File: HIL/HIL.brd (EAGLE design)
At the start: 129.1 x 103.9 mm, 245 parts, among them J1 JTAG_ARM_10PIN, J4 JTAG_ARM_10PIN, U1 CD74HC4067SM96, U10 INA219AIDCNR, U11 INA219AIDCNR, U12 INA219AIDCNR, U14 ADUM1201ARZ, U15 SN65HVD230D, U16 TL1963AKTTR., U17 FT230XS, U2 TL1963AKTTR., U3 CD74HC4067SM96, U4 CD74HC4067SM96, U5 MCP4725A0T-E/CH, U6 TL1963AKTTR., U7 MCP2003-E/SN, U8 TM4C1294NCPDT, U9 INA219AIDCNR, X1 A1944-50, X2 A1944-50, X4 A1944-50, Y3 NX3225GA

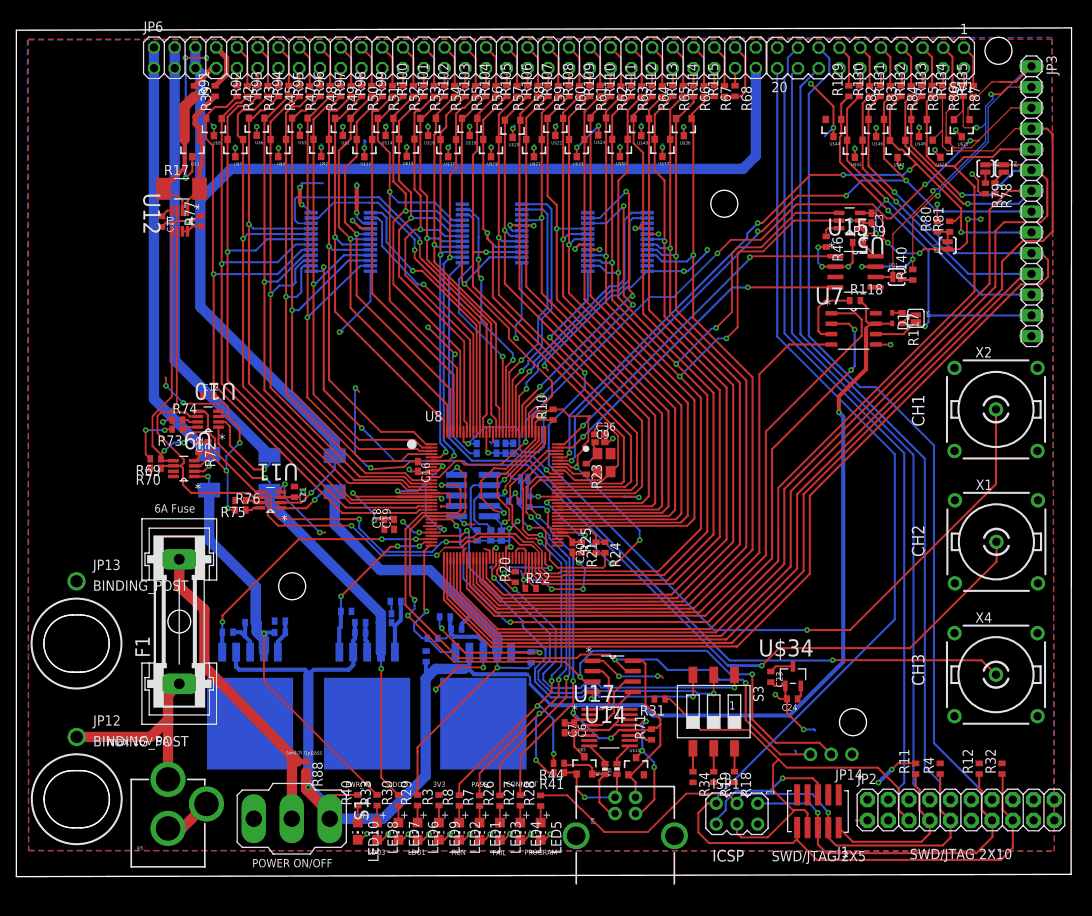
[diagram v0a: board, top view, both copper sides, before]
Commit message: Extend plane
Extend TSTR_3V3’s plane
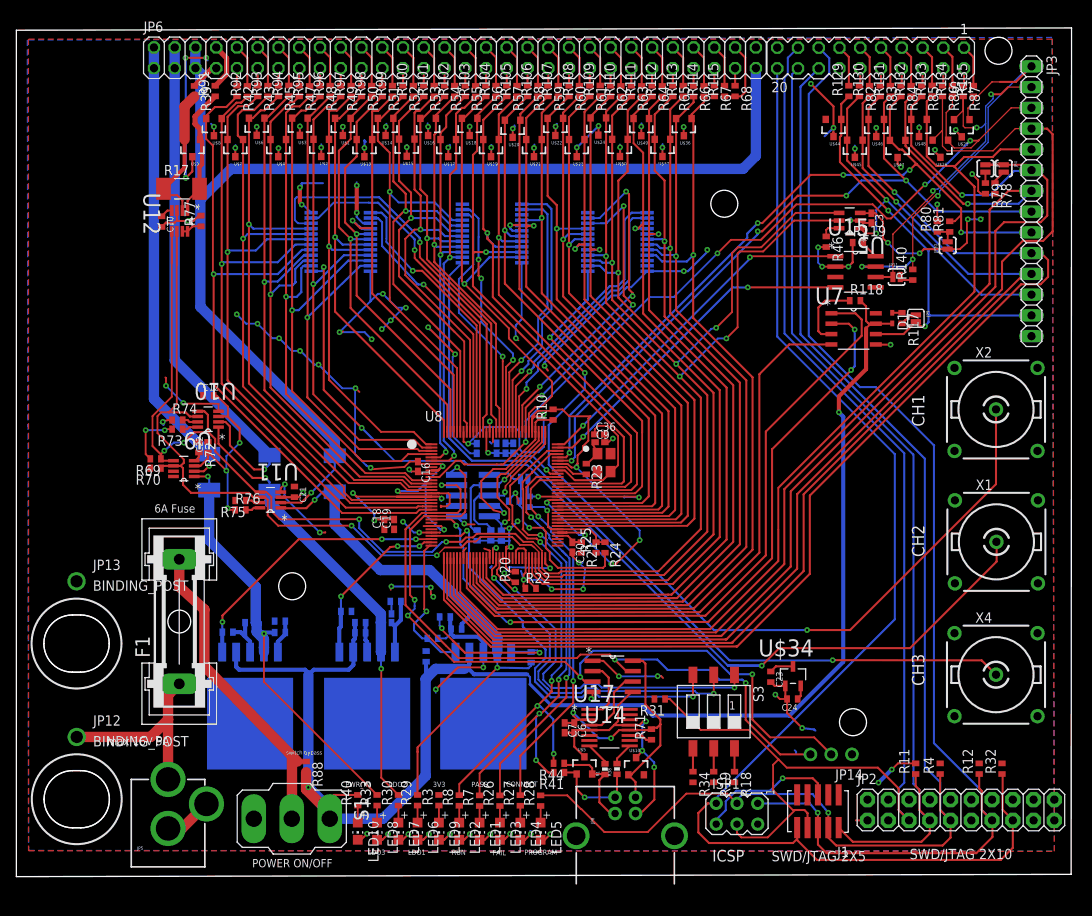
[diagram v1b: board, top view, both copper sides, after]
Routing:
- net TSTR_3V3: track 273.5 -> 312.2 mm, vias 38 -> 51
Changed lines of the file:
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@@
 <wire x1="70.5104" y1="22.1488" x2="70.358" y2="21.9964" width="0.2286" layer="1"/>
 <wire x1="94.3206" y1="21.971" x2="94.3206" y2="20.2588" width="0.254" layer="1"/>
-<wire x1="94.3206" y1="20.2588" x2="96.3422" y2="18.2372" width="0.254" layer="1"/>
-<via x="96.3422" y="18.2372" extent="1-16" drill="0.3048"/>
-<wire x1="96.3422" y1="18.2372" x2="97.6376" y2="18.2372" width="0.254" layer="16"/>
+<wire x1="94.3206" y1="20.2588" x2="96.1644" y2="18.415" width="0.254" layer="1"/>
+<via x="96.1644" y="18.415" extent="1-16" drill="0.3048"/>
+<wire x1="96.1644" y1="18.415" x2="97.6376" y2="18.2372" width="0.254" layer="16"/>
 <wire x1="97.6376" y1="18.2372" x2="97.79" y2="18.0848" width="0.254" layer="16"/>
 <wire x1="23.8252" y1="92.3544" x2="24.1808" y2="91.9988" width="0.254" layer="16"/>
@@
 <wire x1="50.8" y1="49.1368" x2="51.7784" y2="49.1368" width="0.2286" layer="1"/>
 <wire x1="51.7784" y1="49.1368" x2="53.7718" y2="51.1302" width="0.2286" layer="1"/>
-<wire x1="62.3316" y1="53.4162" x2="59.3344" y2="50.673" width="0.2286" layer="1"/>
-<wire x1="59.3344" y1="50.673" x2="54.8132" y2="50.673" width="0.2286" layer="1"/>
+<wire x1="59.3344" y1="50.673" x2="58.801" y2="50.673" width="0.2286" layer="1"/>
+<wire x1="58.801" y1="50.673" x2="54.8132" y2="50.673" width="0.2286" layer="1"/>
 <wire x1="91.1098" y1="78.1558" x2="95.4532" y2="82.4992" width="0.254" layer="1"/>
 <wire x1="62.3316" y1="53.4162" x2="62.3316" y2="55.9816" width="0.254" layer="16"/>
 <wire x1="62.3316" y1="55.9816" x2="62.5856" y2="56.2356" width="0.254" layer="16"/>
+<wire x1="62.3316" y1="53.4162" x2="59.5884" y2="50.673" width="0.2286" layer="1"/>
+<wire x1="59.5884" y1="50.673" x2="59.3344" y2="50.673" width="0.2286" layer="1"/>
 </signal>
 <signal name="DUT_CONNECT">
@@
 <wire x1="63.5254" y1="54.6622" x2="63.5254" y2="53.721" width="0.2286" layer="1"/>
 <wire x1="63.5254" y1="53.721" x2="59.9186" y2="50.1142" width="0.2286" layer="1"/>
-<wire x1="59.9186" y1="50.1142" x2="58.4708" y2="50.2158" width="0.2286" layer="1"/>
-<wire x1="58.4708" y1="50.2158" x2="56.896" y2="48.641" width="0.2286" layer="1"/>
+<wire x1="58.3692" y1="50.1142" x2="56.896" y2="48.641" width="0.2286" layer="1"/>
 <wire x1="57.88151875" y1="45.593" x2="59.055" y2="45.593" width="0.2286" layer="16"/>
 <wire x1="59.055" y1="45.593" x2="59.69" y2="44.7294" width="0.2286" layer="16"/>
@@
 <wire x1="58.42" y1="45.0596" x2="56.896" y2="46.5836" width="0.2286" layer="1"/>
 <wire x1="56.896" y1="46.5836" x2="56.896" y2="48.641" width="0.2286" layer="1"/>
+<wire x1="59.9186" y1="50.1142" x2="58.3692" y2="50.1142" width="0.2286" layer="1"/>
 </signal>
 <signal name="TARGET_TMS/SWDIO">
@@
 <wire x1="61.0616" y1="37.5562" x2="60.4624" y2="37.5562" width="0.2286" layer="1"/>
 <wire x1="60.4624" y1="37.5562" x2="59.9186" y2="38.1" width="0.2286" layer="1"/>
+<via x="51.0286" y="34.4678" extent="1-16" drill="0.3048"/>
+<wire x1="51.0286" y1="34.4678" x2="50.7238" y2="34.7726" width="0.2286" layer="1"/>
+<wire x1="50.7238" y1="34.7726" x2="50.7238" y2="35.6108" width="0.2286" layer="1"/>
+<via x="50.7238" y="35.6108" extent="1-16" drill="0.3048"/>
+<wire x1="50.7238" y1="35.6108" x2="50.5968" y2="35.7378" width="0.2286" layer="16"/>
+<wire x1="50.5968" y1="35.7378" x2="45.8978" y2="35.7378" width="0.2286" layer="16"/>
+<via x="45.8978" y="35.7378" extent="1-16" drill="0.3048"/>
+<wire x1="45.8978" y1="35.7378" x2="45.8216" y2="35.6616" width="0.2286" layer="1"/>
+<wire x1="45.8216" y1="35.6616" x2="45.8216" y2="35.3314" width="0.2286" layer="1"/>
+<via x="36.9824" y="62.8904" extent="1-16" drill="0.3048"/>
+<via x="34.7218" y="64.5668" extent="1-16" drill="0.3048"/>
+<via x="32.1564" y="66.1162" extent="1-16" drill="0.3048"/>
+<via x="29.5148" y="67.8942" extent="1-16" drill="0.3048"/>
+<via x="26.9748" y="69.0372" extent="1-16" drill="0.3048"/>
+<wire x1="26.9748" y1="69.0372" x2="28.1178" y2="67.8942" width="0.2286" layer="16"/>
+<wire x1="28.1178" y1="67.8942" x2="29.5148" y2="67.8942" width="0.2286" layer="16"/>
+<wire x1="29.5148" y1="67.8942" x2="31.2928" y2="66.1162" width="0.2286" layer="16"/>
+<wire x1="31.2928" y1="66.1162" x2="32.1564" y2="66.1162" width="0.2286" layer="16"/>
+<wire x1="32.1564" y1="66.1162" x2="32.1564" y2="66.1416" width="0.2286" layer="16"/>
+<wire x1="32.1564" y1="66.1416" x2="33.7312" y2="64.5668" width="0.2286" layer="16"/>
+<wire x1="33.7312" y1="64.5668" x2="34.7218" y2="64.5668" width="0.2286" layer="16"/>
+<wire x1="34.7218" y1="64.5668" x2="34.7472" y2="64.5922" width="0.2286" layer="16"/>
+<wire x1="34.7472" y1="64.5922" x2="36.449" y2="62.8904" width="0.2286" layer="16"/>
+<wire x1="36.449" y1="62.8904" x2="36.9824" y2="62.8904" width="0.2286" layer="16"/>
+<wire x1="36.9824" y1="62.8904" x2="39.878" y2="59.9948" width="0.2286" layer="16"/>
+<wire x1="39.878" y1="59.9948" x2="41.5036" y2="59.9948" width="0.2286" layer="16"/>
+<via x="47.6758" y="69.85" extent="1-16" drill="0.3048"/>
+<via x="44.8564" y="71.5518" extent="1-16" drill="0.3048"/>
+<via x="45.8216" y="68.3006" extent="1-16" drill="0.3048"/>
+<via x="44.7294" y="67.2338" extent="1-16" drill="0.3048"/>
+<via x="43.4848" y="65.9892" extent="1-16" drill="0.3048"/>
+<wire x1="43.3324" y1="70.6374" x2="44.2468" y2="71.5518" width="0.2286" layer="16"/>
+<wire x1="44.2468" y1="71.5518" x2="44.8564" y2="71.5518" width="0.2286" layer="16"/>
+<wire x1="44.8564" y1="71.5518" x2="46.5582" y2="69.85" width="0.2286" layer="16"/>
+<wire x1="46.5582" y1="69.85" x2="47.6758" y2="69.85" width="0.2286" layer="16"/>
+<wire x1="45.8216" y1="68.3006" x2="47.371" y2="69.85" width="0.2286" layer="16"/>
+<wire x1="47.371" y1="69.85" x2="47.6758" y2="69.85" width="0.2286" layer="16"/>
+<wire x1="45.8216" y1="68.3006" x2="44.7548" y2="67.2338" width="0.2286" layer="16"/>
+<wire x1="44.7548" y1="67.2338" x2="44.7294" y2="67.2338" width="0.2286" layer="16"/>
+<wire x1="43.4848" y1="65.9892" x2="42.6212" y2="66.8528" width="0.2286" layer="16"/>
+<wire x1="42.6212" y1="66.8528" x2="39.5478" y2="66.8528" width="0.2286" layer="16"/>
 </signal>
 <signal name="LDO1_SH+" class="5">
@@
 <via x="90.0684" y="24.9936" extent="1-16" drill="0.3048"/>
 <wire x1="90.0684" y1="24.9936" x2="90.0684" y2="19.4564" width="0.254" layer="1"/>
-<wire x1="90.0684" y1="19.4564" x2="91.3892" y2="18.1356" width="0.254" layer="1"/>
-<wire x1="91.3892" y1="18.1356" x2="92.1004" y2="17.4244" width="0.254" layer="1"/>
 <wire x1="99.7204" y1="15.1892" x2="98.298" y2="16.6116" width="0.254" layer="1"/>
-<wire x1="98.298" y1="16.6116" x2="92.9132" y2="16.6116" width="0.254" layer="1"/>
-<wire x1="92.9132" y1="16.6116" x2="92.1004" y2="17.4244" width="0.254" layer="1"/>
+<wire x1="92.2528" y1="17.272" x2="90.0684" y2="19.4564" width="0.254" layer="1"/>
+<wire x1="98.298" y1="16.6116" x2="97.6376" y2="17.272" width="0.2286" layer="1"/>
+<wire x1="97.6376" y1="17.272" x2="92.2528" y2="17.272" width="0.2286" layer="1"/>
 </signal>
 <signal name="HOST_UART_TX">
@@
 <contactref element="U8" pad="P$2"/>
 <contactref element="U1" pad="21"/>
-<wire x1="36.3626" y1="72.7456" x2="36.3626" y2="90.4588" width="0.254" layer="1"/>
-<wire x1="36.3626" y1="59.2684" x2="41.9481" y2="53.6829" width="0.2286" layer="1"/>
+<wire x1="36.3372" y1="72.7456" x2="36.3626" y2="90.4588" width="0.254" layer="1"/>
+<wire x1="36.3372" y1="59.2684" x2="41.9481" y2="53.6829" width="0.2286" layer="1"/>
 <wire x1="50.8" y1="52.7368" x2="49.6506" y2="52.7368" width="0.2286" layer="1"/>
 <wire x1="49.6506" y1="52.7368" x2="48.7045" y2="53.6829" width="0.2286" layer="1"/>
@@
 <wire x1="43.3324" y1="76.2762" x2="40.0964" y2="76.2762" width="0.254" layer="16"/>
 <wire x1="40.0964" y1="76.2762" x2="36.3626" y2="72.5424" width="0.254" layer="16"/>
-<wire x1="36.3626" y1="72.5424" x2="36.3626" y2="72.7456" width="0.254" layer="16"/>
-<via x="36.3626" y="72.7456" extent="1-16" drill="0.3048"/>
+<wire x1="36.3626" y1="72.5424" x2="36.3372" y2="72.7456" width="0.254" layer="16"/>
+<via x="36.3372" y="72.7456" extent="1-16" drill="0.3048"/>
 <wire x1="39.7002" y1="95.7176" x2="38.4198" y2="94.4372" width="0.254" layer="1"/>
 <wire x1="38.4198" y1="94.4372" x2="37.9222" y2="94.4372" width="0.254" layer="1"/>
 <wire x1="37.9222" y1="94.4372" x2="36.3626" y2="92.8776" width="0.254" layer="1"/>
 <wire x1="36.3626" y1="92.8776" x2="36.3626" y2="90.4588" width="0.254" layer="1"/>
-<wire x1="36.3626" y1="59.2684" x2="36.3626" y2="72.7456" width="0.254" layer="1"/>
+<wire x1="36.3372" y1="59.2684" x2="36.3372" y2="72.7456" width="0.254" layer="1"/>
 </signal>
 <signal name="AD9">

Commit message: smal fixes
better 3v3 plane coverage
add labels
fix tracks which are not straight or 45 degree
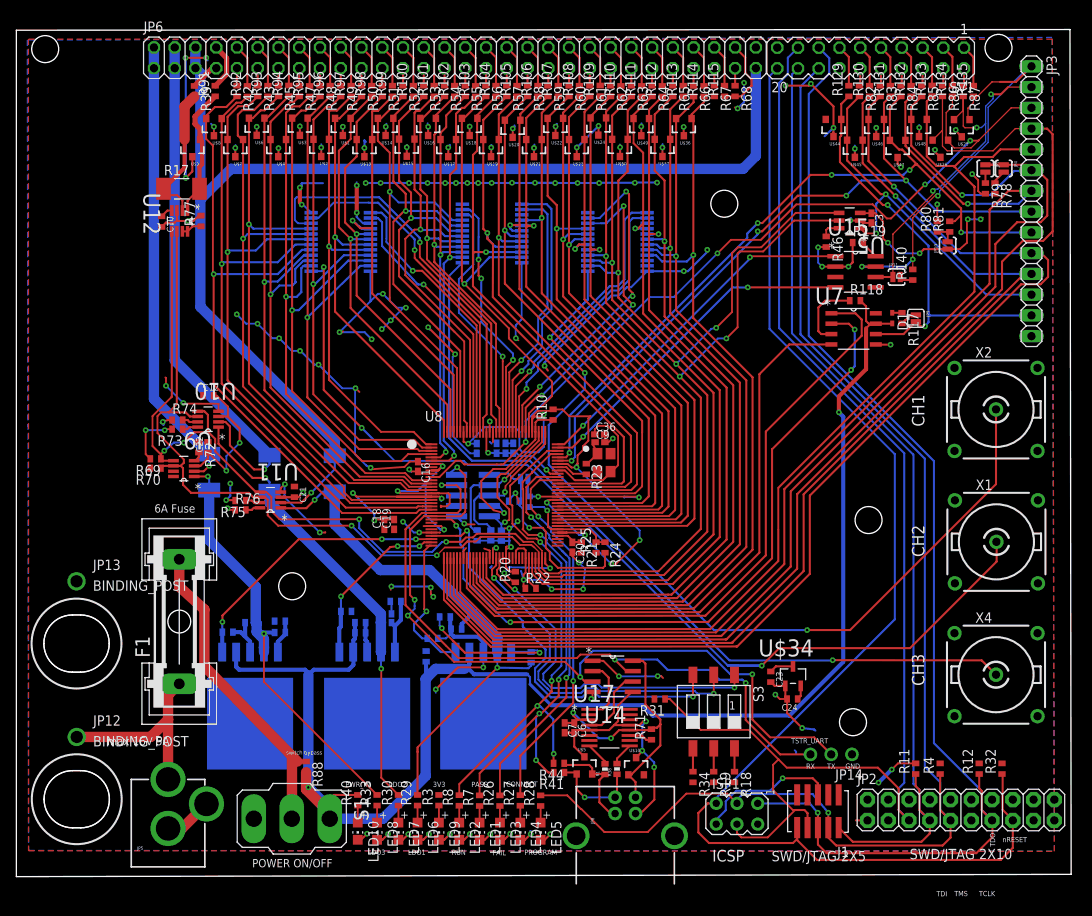
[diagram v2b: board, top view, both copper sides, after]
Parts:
- added STANDOFF3, STANDOFF4: STAND-OFF, SparkFun-Electromechanical:STAND-OFF
- moved STANDOFF2 0.36 mm to (120.2, 101.7)
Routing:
- net TSTR_3V3: track 312.2 -> 357.8 mm, vias 51 -> 71
- net SWO/TDO/MOSI: track 149.4 -> 148.2 mm
- net DUT_CS: track 149.9 -> 149.0 mm
- net NRESET: track 162.0 -> 162.7 mm
- net DUT_AOUT1: track 44.7 -> 45.3 mm
- net GND: track 333.7 -> 333.1 mm, vias 81 -> 82
- net TDI/MISO: track 161.2 -> 161.7 mm
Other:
- board size 129.1 x 103.9 mm -> 129.1 x 103.7 mm
- board text added: "GND"
- board text added: "RX"
- board text added: "TCLK"
- board text added: "TDI"
- board text added: "TDO"
- board text added: "TMS"
- board text added: "TSTR_UART"
- board text added: "TX"
- board text added: "nRESET"
